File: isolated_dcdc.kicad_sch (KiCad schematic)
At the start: 15 parts, among them U6 LMR51610, U7 NXE2S0505MC, U8 NCP1117-3.3_SOT223

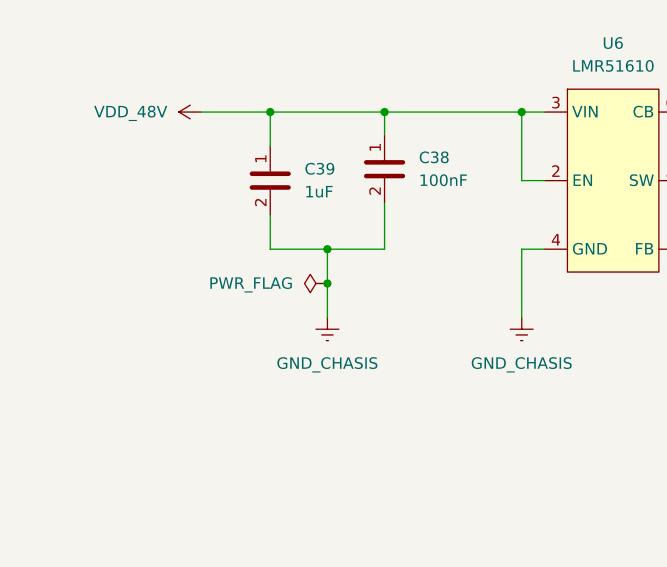
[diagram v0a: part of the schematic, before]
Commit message: fix: cleaned up DRC and ERC's for major errors
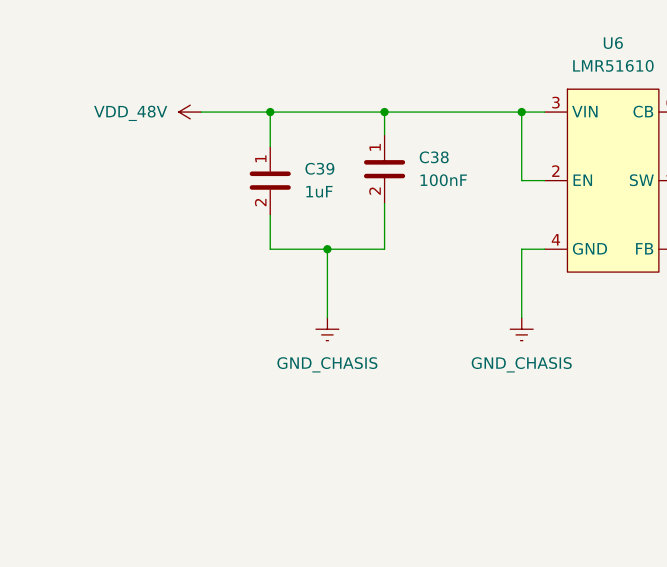
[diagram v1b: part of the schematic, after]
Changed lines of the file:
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@@
-	)
-	(junction
-		(at 46.99 107.95)
-		(diameter 0)
-		(color 0 0 0 0)
 	)
 	(junction
@@
 		)
 	)
-	(wire
-		(pts
-			(xy 46.99 107.95) (xy 46.99 111.76)
-		)
-		(stroke
-			(width 0)
-			(type default)
-		)
-	)
 	(polyline
 		(pts
@@
 	(wire
 		(pts
-			(xy 46.99 104.14) (xy 46.99 107.95)
+			(xy 46.99 104.14) (xy 46.99 111.76)
 		)
 		(stroke
@@
 					(unit 1)
 				)
-			)
-		)
-	)
-	(symbol
-		(lib_id "power:PWR_FLAG")
-		(at 46.99 107.95 90)
-		(unit 1)
-		(body_style 1)
-		(exclude_from_sim no)
-		(in_bom yes)
-		(on_board yes)
-		(in_pos_files yes)
-		(dnp no)
-		(fields_autoplaced yes)
-		(property "Reference" "#FLG5"
-			(at 45.085 107.95 0)
-			(hide yes)
-			(show_name no)
-			(do_not_autoplace no)
-			(effects
-				(font
-					(size 1.27 1.27)
-				)
-			)
-		)
-		(property "Value" "PWR_FLAG"
-			(at 43.18 107.9499 90)
-			(show_name no)
-			(do_not_autoplace no)
-			(effects
-				(font
-					(size 1.27 1.27)
-				)
-				(justify left)
-			)
-		)
-		(property "Footprint" ""
-			(at 46.99 107.95 0)
-			(hide yes)
-			(show_name no)
-			(do_not_autoplace no)
-			(effects
-				(font
-					(size 1.27 1.27)
-				)
-			)
-		)
-		(property "Datasheet" ""
-			(at 46.99 107.95 0)
-			(hide yes)
-			(show_name no)
-			(do_not_autoplace no)
-			(effects
-				(font
-					(size 1.27 1.27)
-				)
-			)
-		)
-		(property "Description" "Special symbol for telling ERC where power comes from"
-			(at 46.99 107.95 0)
-			(hide yes)
-			(show_name no)
-			(do_not_autoplace no)
-			(effects
-				(font
-					(size 1.27 1.27)
-				)
-			)
-		)
-		(pin "1"
-		)
-		(instances
-			(project "Rover VCU"
-				(path "/33c96268-4ca2-4a73-94d6-a3ed4f27d429/1a57b0d4-5d08-45a2-8c8c-1ccd6aae71a7"
-					(reference "#FLG5")
-					(unit 1)
-				)
